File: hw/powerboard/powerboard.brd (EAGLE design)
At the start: 100 x 80 mm, 37 parts, among them J1 ISP, J2 I2C

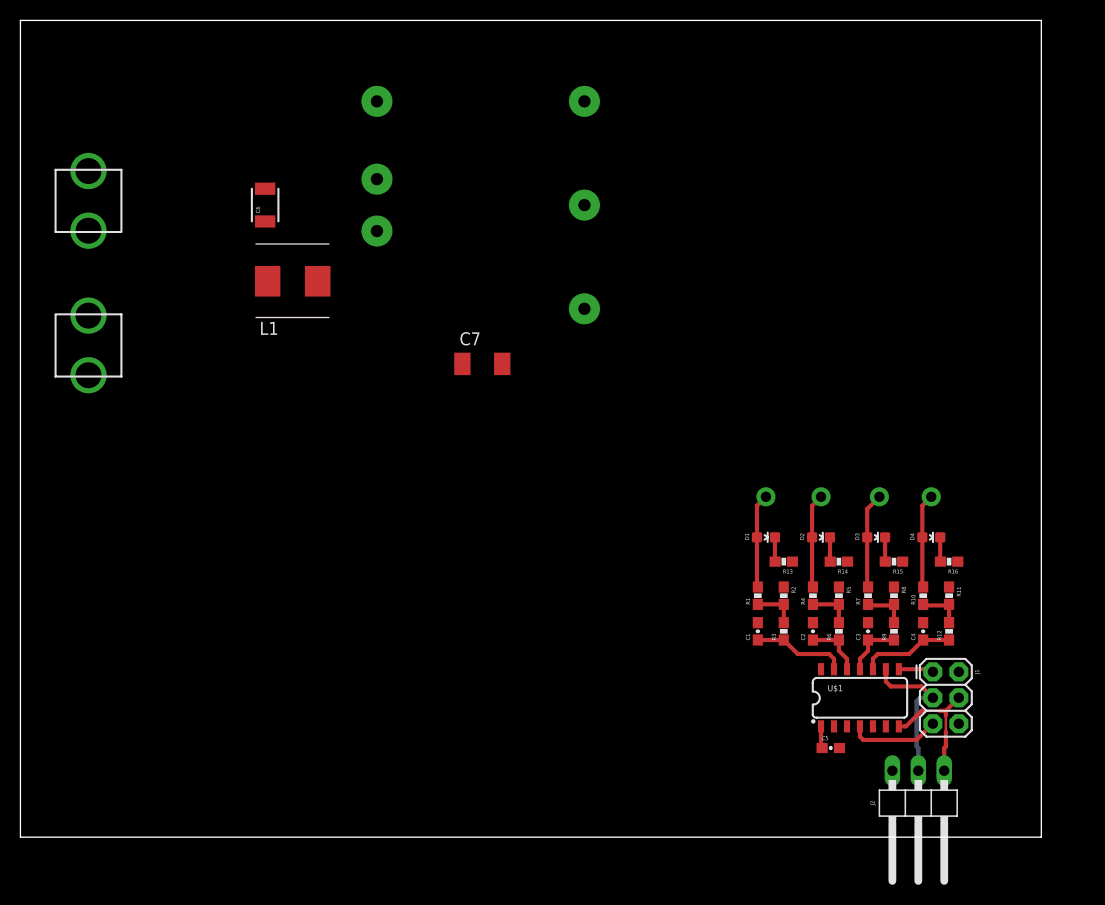
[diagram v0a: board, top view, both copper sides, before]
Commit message: Fixed AXA DC/DC module
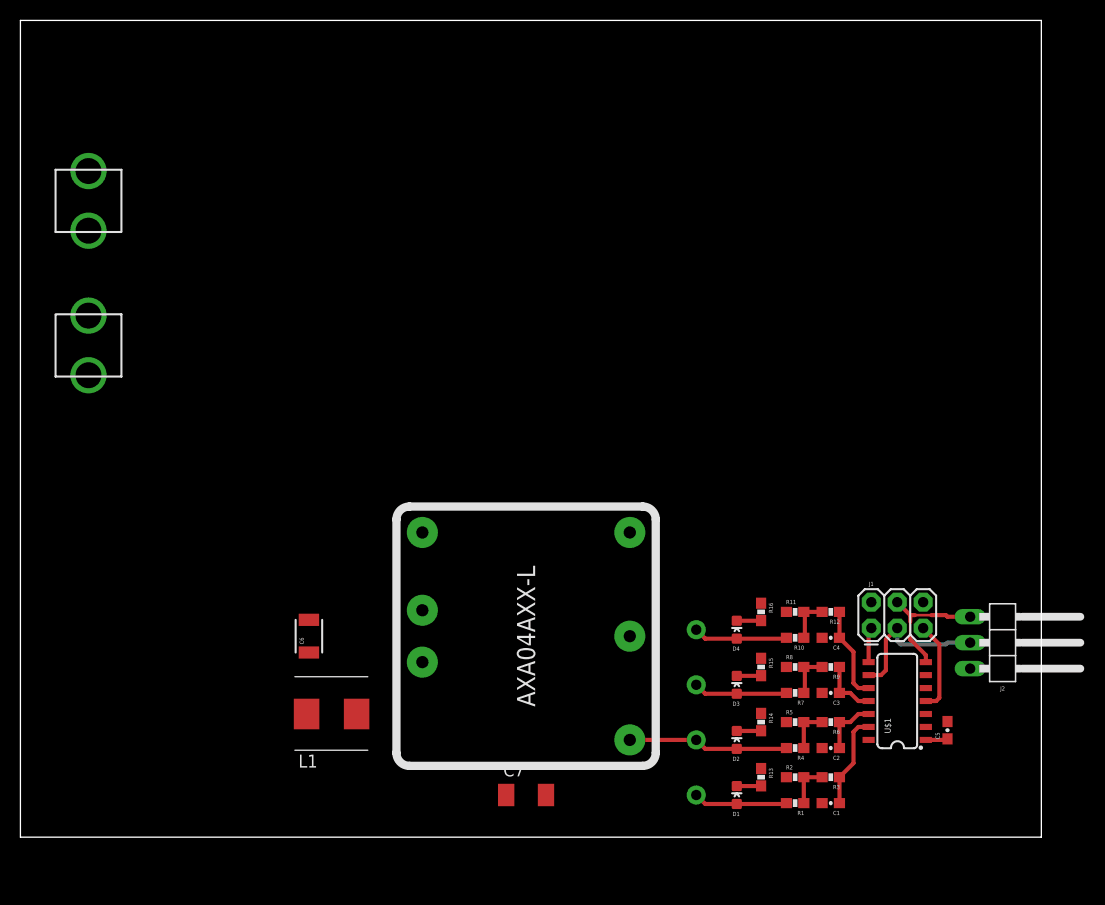
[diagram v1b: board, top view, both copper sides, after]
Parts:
- moved L1 42.6 mm to (30.5, 12.1)
- moved U$2 42.5 mm to (49.5, 19.7), flipped to the top, turned to 270 degrees
- moved C6 42.4 mm to (28.3, 19.7)
- moved C7 42.4 mm to (49.5, 4.13)
- moved J3 30.0 mm to (66.2, 4.13), turned to 180 degrees
- moved J4 26.8 mm to (66.2, 9.53), turned to 90 degrees
- moved J6 26.4 mm to (66.2, 20.3), turned to 90 degrees
- moved J5 25.7 mm to (66.2, 14.9), turned to 180 degrees
- moved D1 25.4 mm to (70.2, 4.13), turned to 0 degrees
- moved D2 21.5 mm to (70.2, 9.53), turned to 0 degrees
- moved R13 21.2 mm to (72.5, 5.87), turned to 270 degrees
- moved D4 21.1 mm to (70.2, 20.3), turned to 0 degrees
- moved R1 20.6 mm to (75.9, 3.33), turned to 180 degrees
- moved D3 19.9 mm to (70.2, 14.9), turned to 0 degrees
- moved R16 19.1 mm to (72.5, 22.1), turned to 270 degrees
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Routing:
- net 5V: track 11.4 -> 18.0 mm

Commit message: Recent progress with powerboard schematics
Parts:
- added BATTERY: (no value), con-wago-500:W237-102
- added Q1: IRF4905, transistor-power:TO220BH
- D1: value BAT -> BATT
- moved J2 69.7 mm to (28.1, 7.30), turned to 180 degrees
- moved C5 54.1 mm to (37.0, 5.24), turned to 0 degrees
- moved C1 51.3 mm to (29.8, 16.7), turned to 90 degrees
- moved R1 49.0 mm to (29.8, 20.2), turned to 90 degrees
- moved R3 48.2 mm to (32.4, 16.7), turned to 90 degrees
- moved U$1 46.1 mm to (39.8, 10.2), turned to 0 degrees
- moved R2 45.8 mm to (32.4, 20.2), turned to 270 degrees
- moved D1 45.1 mm to (30.6, 25.9), turned to 270 degrees
- moved C2 44.8 mm to (35.2, 16.7), turned to 90 degrees
- moved J3 43.9 mm to (30.6, 29.8), turned to 90 degrees
- moved R13 43.9 mm to (32.4, 23.5), turned to 180 degrees
- moved R4 42.2 mm to (35.2, 20.2), turned to 90 degrees
- moved R6 41.9 mm to (37.8, 16.7), turned to 90 degrees
- moved F1 40.6 mm to (6.19, 14.6)
- moved R5 39.1 mm to (37.8, 20.2), turned to 270 degrees
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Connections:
- net V_BATT_ADC renamed 12V_ADC
- removed net V_BATT: C6.1, D1.A, F1.3, J3.1, L1.1, R1.2
- new net 12V: C6.1, D1.A, J3.1, L1.1, Q1.S, R1.2
- new net N$11: BATTERY.1, F1.3
- new net N$9: F1.1, Q1.D
- net GND: now also BATTERY.2, Q1.G
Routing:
- net 12V: track 0.00 -> 9.28 mm
- net V_BATT: track 9.28 -> 0.00 mm
- net SDA/MOSI: track 13.0 -> 22.2 mm
- net SCK: track 15.1 -> 23.3 mm
- net 5V: track 18.0 -> 11.4 mm

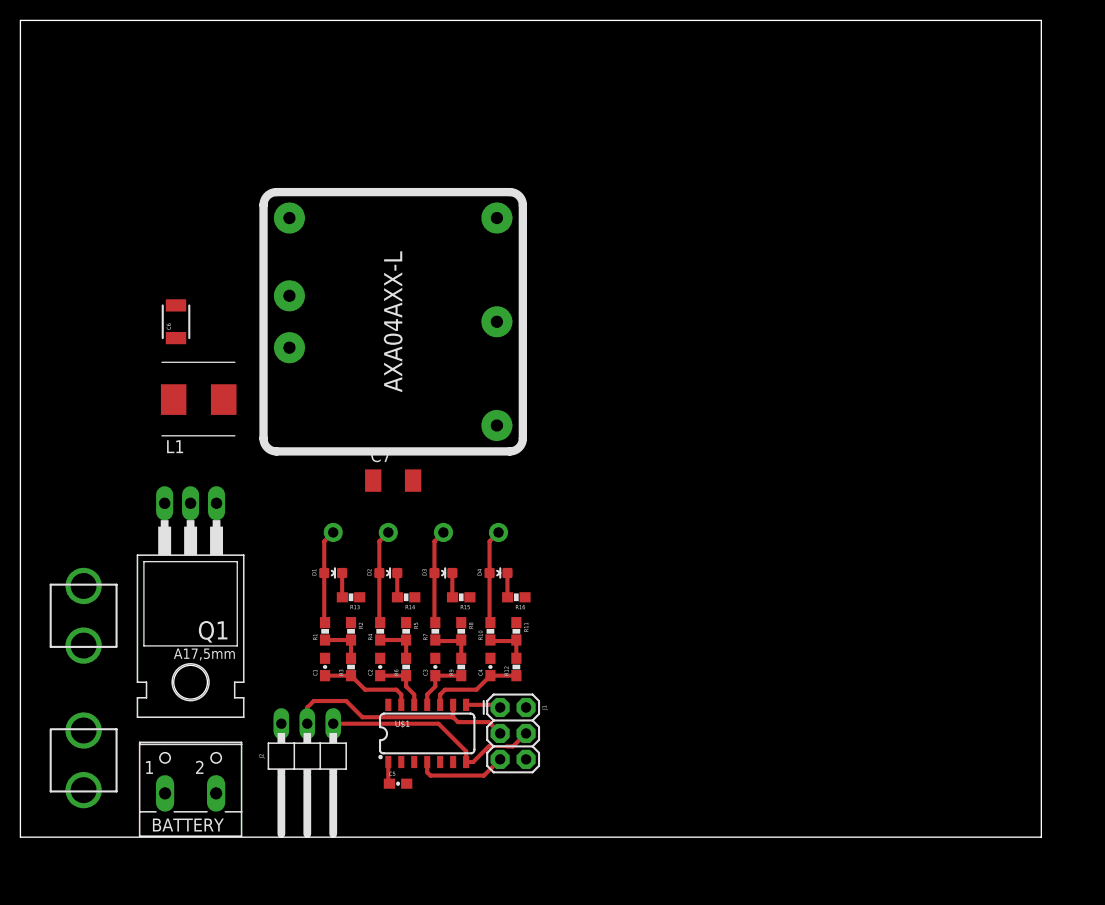
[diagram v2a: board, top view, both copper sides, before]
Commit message: Added N-channel MOSFET and TVS-diode to powerboard
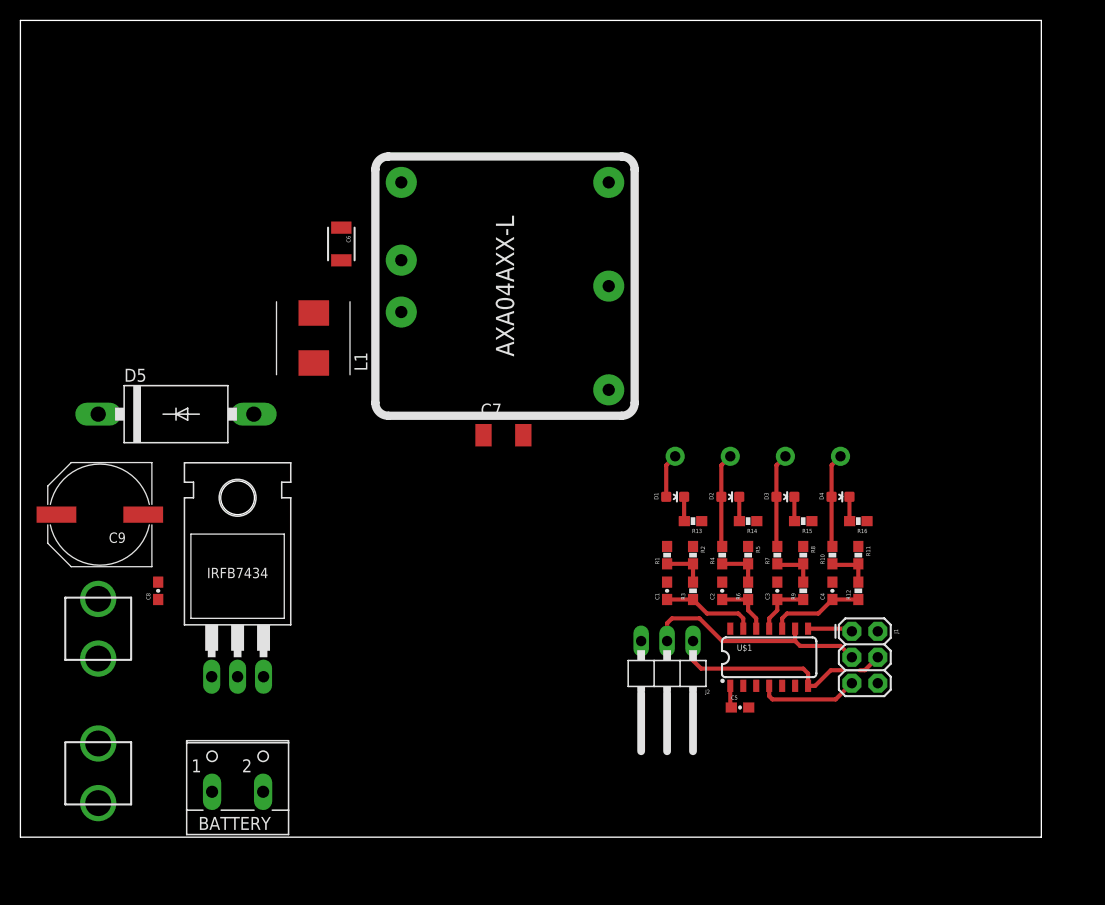
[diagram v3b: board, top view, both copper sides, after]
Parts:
- removed Q1: IRF4905, transistor-power:TO220BH
- added C8: 0.1uF, SparkFun-Capacitors:0603-CAP
- added C9: 220uF, rcl:PANASONIC_G
- added D5: 1N6277A, powerboard:1N6277A
- added U$3: IRFB7434PBF, powerboard:IRFB7434PBF
- moved J2 36.2 mm to (63.3, 15.4)
- moved J1 35.2 mm to (81.4, 20.2)
- moved C1 34.3 mm to (63.3, 24.1)
- moved C3 34.3 mm to (74.1, 24.1)
- moved D1 34.3 mm to (64.1, 33.3)
- moved D3 34.3 mm to (74.9, 33.3)
- moved D4 34.3 mm to (80.3, 33.3)
- moved J3 34.3 mm to (64.1, 37.3)
- moved J5 34.3 mm to (74.9, 37.3)
- moved J6 34.3 mm to (80.3, 37.3)
- moved R1 34.3 mm to (63.3, 27.6)
- moved R11 34.3 mm to (82.1, 27.6)
- moved R12 34.3 mm to (82.1, 24.1)
- moved R14 34.3 mm to (71.3, 31.0)
- moved R16 34.3 mm to (82.1, 31.0)
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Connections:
- removed net 12V: C6.1, D1.A, J3.1, L1.1, Q1.S, R1.2
- removed net N$9: F1.1, Q1.D
- new net N$12: BATTERY.2, C8.2, C9.-, U$3.DRAIN
- new net V_BATT: C6.1, C8.1, C9.+, D1.A, D5.C, F1.1, J3.1, L1.1, R1.2, U$3.GATE
- net GND: now also D5.A, U$3.SOURCE; no longer BATTERY.2, Q1.G
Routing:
- net 12V: track 9.28 -> 0.00 mm
- net V_BATT: track 0.00 -> 4.42 mm
- net MISO: track 3.44 -> 4.39 mm
- net RESET: track 8.94 -> 9.90 mm
- net SDA/MOSI: track 22.2 -> 22.9 mm

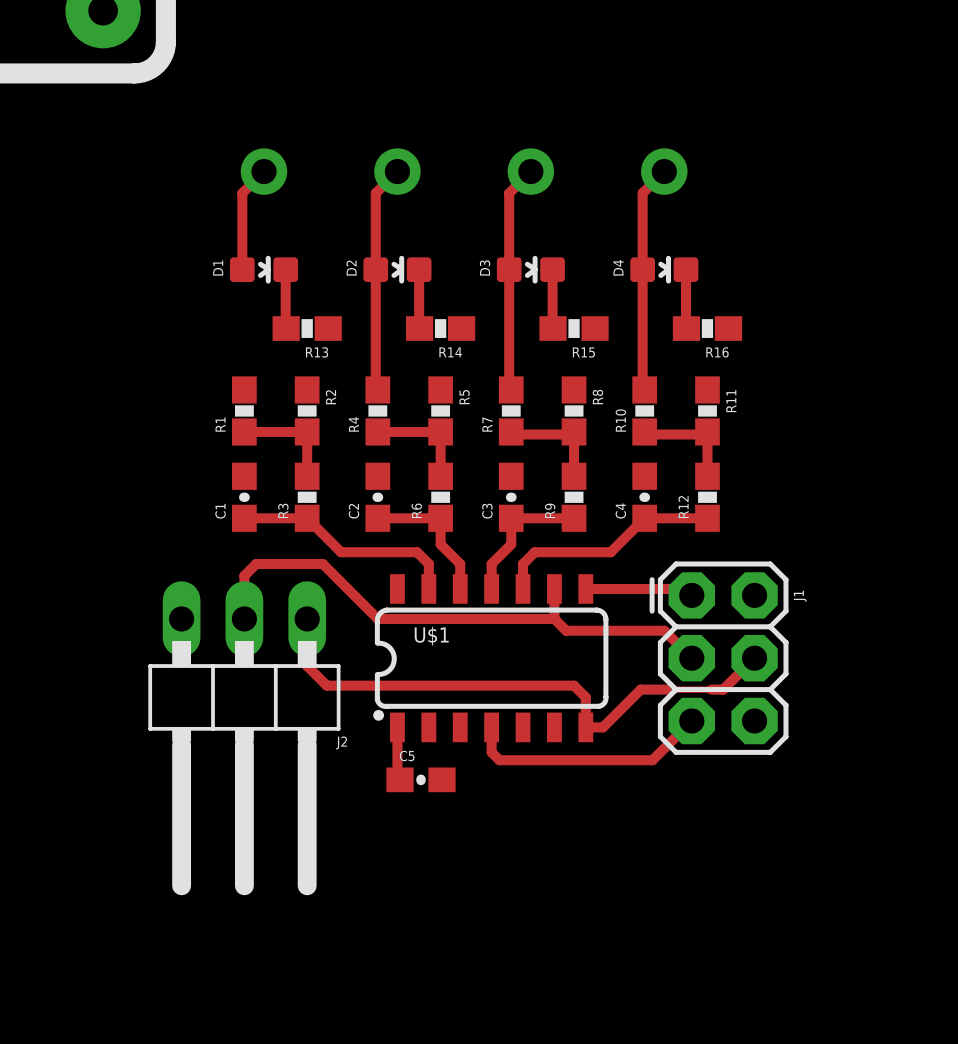
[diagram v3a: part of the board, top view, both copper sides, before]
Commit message: Initial commit of PowerSensor board. Decided to separate PowerBoard and PowerSensor.
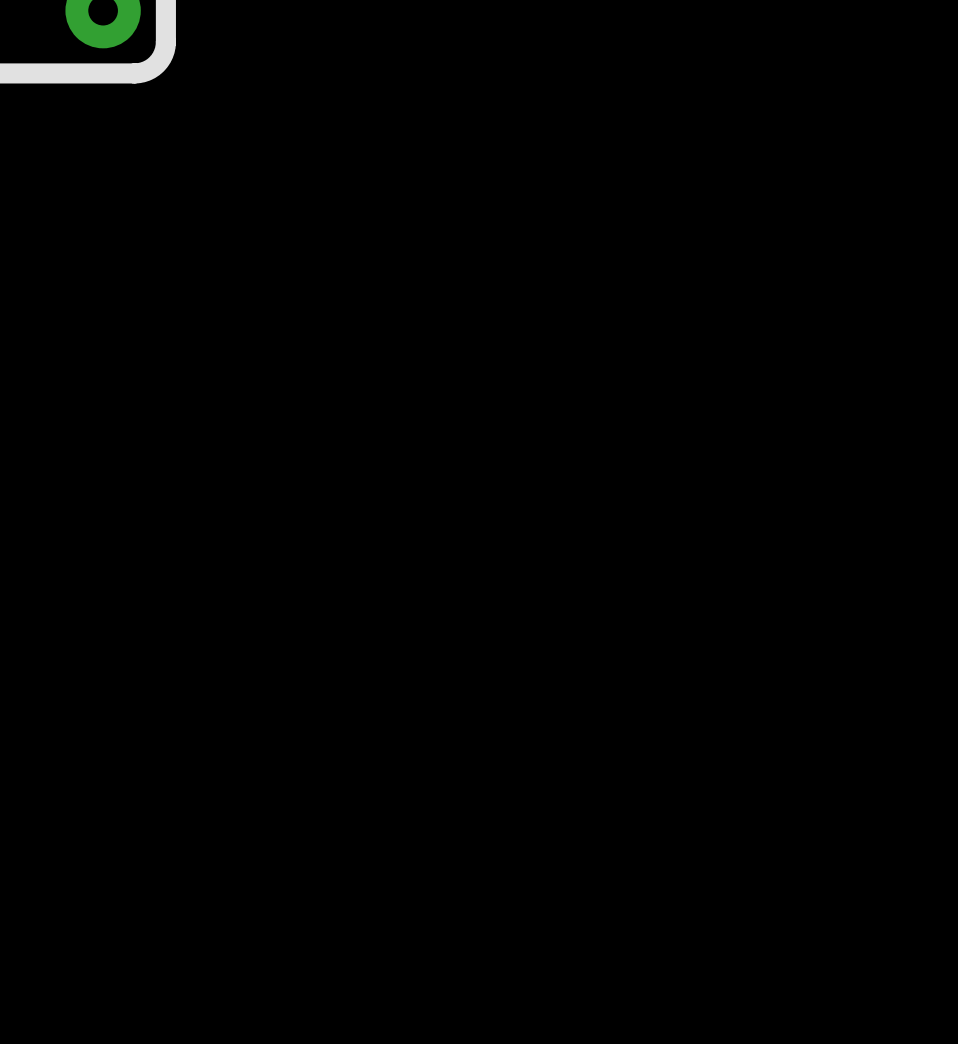
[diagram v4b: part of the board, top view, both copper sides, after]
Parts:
- removed C1, C2, C3, C4: (no value), SparkFun-Capacitors:0603-CAP
- removed C5: 100nF, SparkFun-Capacitors:0603-CAP
- removed D1: BATT, SparkFun-LED:LED-0603
- removed D2: 5V, SparkFun-LED:LED-0603
- removed D3: 3.3V, SparkFun-LED:LED-0603
- removed D4: 1.8V, SparkFun-LED:LED-0603
- removed J1: ISP, SparkFun-Connectors:2X3
- removed J2: I2C, pinhead:1X03/90
- removed J3, J4, J5, J6: (no value), SparkFun-Connectors:1X01NS-KIT
- removed R1, R10, R11, R12, R13, R14, R15, R16, R2, R3, R4, R5, R6, R7, R8, R9: (no value), SparkFun-Passives:0603-RES
- removed U$1: ATTINY84, SparkFun-DigitalIC:SO14
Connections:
- removed net 1.8V: D4.A, J6.1, R10.2
- removed net 1.8V_ADC: C4.1, R12.1, U$1.10
- removed net 12V_ADC: C1.1, R3.1, U$1.13
- removed net 3.3V: D3.A, J5.1, R7.2
- removed net 3.3V_ADC: C3.1, R9.1, U$1.11
- removed net 5V_ADC: C2.1, R6.1, U$1.12
- removed net MISO: J1.1, U$1.8
- removed net N$1: R1.1, R2.2, R3.2
- removed net N$2: R4.1, R5.2, R6.2
- removed net N$3: R7.1, R8.2, R9.2
- removed net N$4: R10.1, R11.2, R12.2
- removed net N$5: D1.C, R13.2
- removed net N$6: D2.C, R14.2
- removed net N$7: D3.C, R15.2
- removed net N$8: D4.C, R16.2
- removed net RESET: J1.5, U$1.4
- removed net SCK: J1.3, J2.2, U$1.9
- removed net SDA/MOSI: J1.4, J2.1, U$1.7
- net 5V: no longer C5.1, D2.A, J1.2, J4.1, R4.2, U$1.1
- net GND: no longer C1.2, C2.2, C3.2, C4.2, C5.2, J1.6, J2.3, R11.1, R13.1, R14.1, R15.1, R16.1, R2.1, R5.1, R8.1, U$1.14
- net V_BATT: no longer D1.A, J3.1, R1.2
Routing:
- net SDA/MOSI: track 22.9 -> 0.00 mm
- net SCK: track 22.8 -> 0.00 mm
- net 5V: track 11.4 -> 0.00 mm
- net RESET: track 9.90 -> 0.00 mm
- net 1.8V_ADC: track 9.34 -> 0.00 mm
- net 12V_ADC: track 9.29 -> 0.00 mm
- net 3.3V: track 9.28 -> 0.00 mm
- net 1.8V: track 9.28 -> 0.00 mm
- net 5V_ADC: track 5.73 -> 0.00 mm
- net 3.3V_ADC: track 5.73 -> 0.00 mm
- net N$4: track 4.48 -> 0.00 mm
- net N$3: track 4.48 -> 0.00 mm
- net V_BATT: track 4.42 -> 0.00 mm
- net MISO: track 4.39 -> 0.00 mm
- net N$2: track 4.33 -> 0.00 mm
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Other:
- board text removed: "GND"
- board text removed: "SCK"
- board text removed: "SDA"
